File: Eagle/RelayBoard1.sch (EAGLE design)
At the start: 12 parts, among them IC1 ULN2003AN, J1 POWER, J2 CPU_BOARD, K1 4052, K2 4052, K3 4051, X1 MKDSN1,5/6-5,08, X2 MKDSN1,5/6-5,08, X4 MKDSN1,5/3-5,08

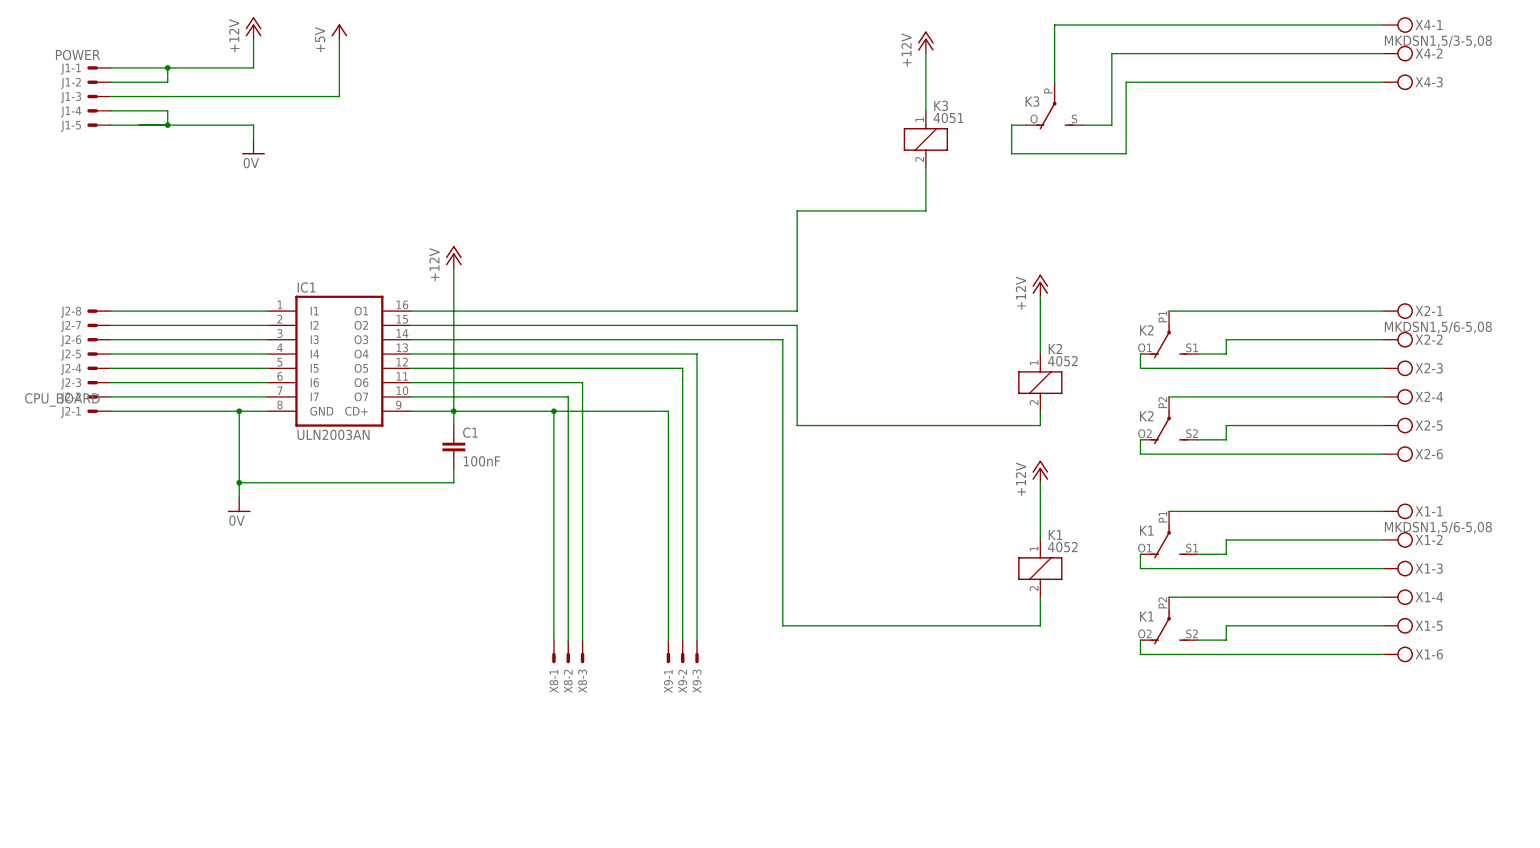
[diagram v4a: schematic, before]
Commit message: - cabling of RelayBoard1 partly changed - some pin-swaps to ButtonBoard -> blrtest.c finally works as expected
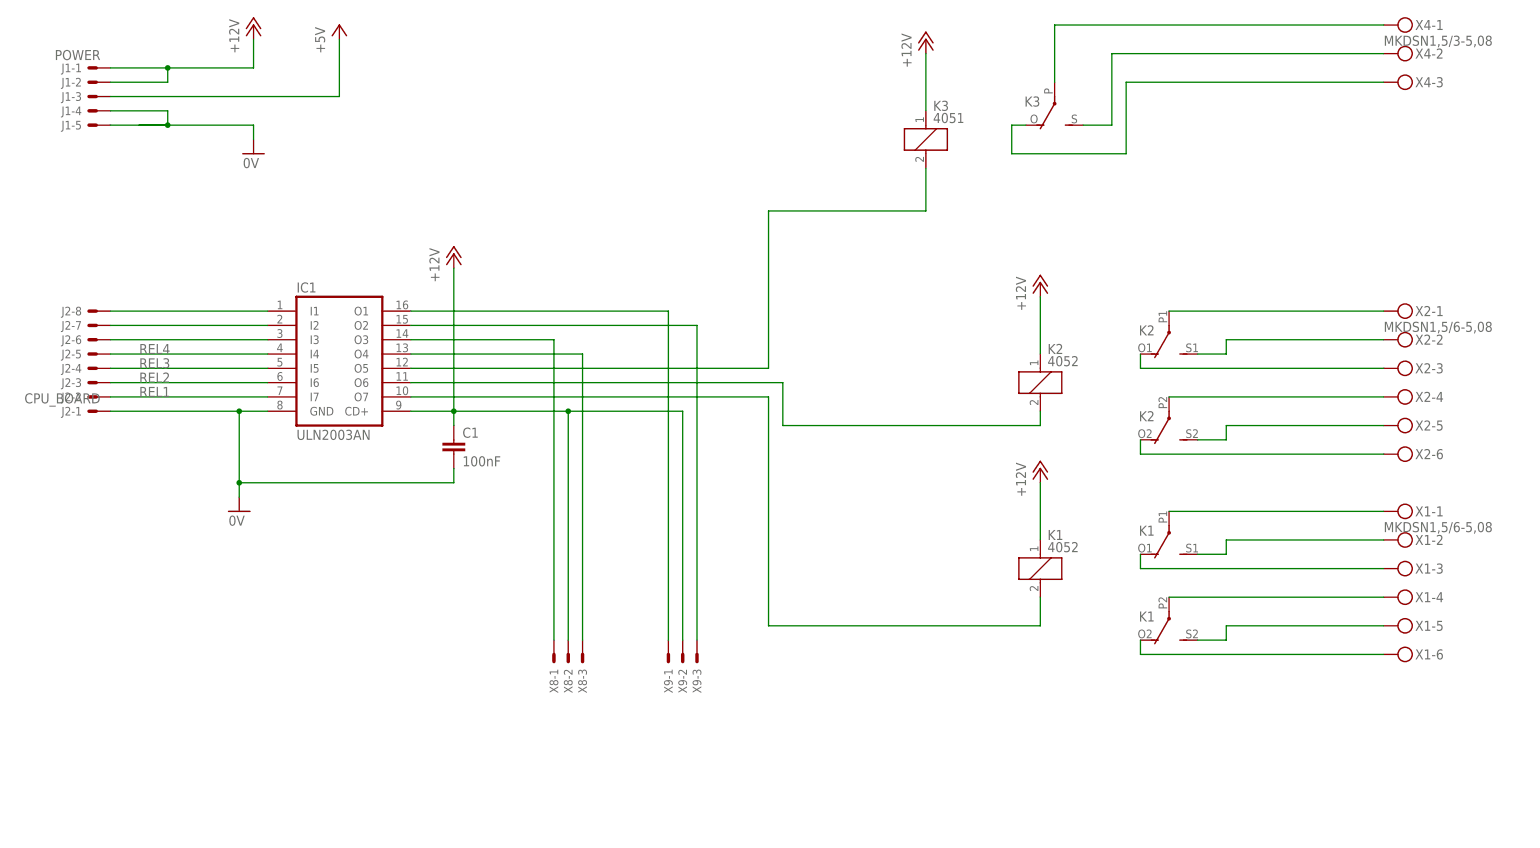
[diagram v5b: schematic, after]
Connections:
- net N$20 renamed REL4
- net N$21 renamed REL3
- net N$22 renamed REL2
- net N$23 renamed REL1
- net +12V: now also X8-2.S, X9-2.S; no longer X8-1.S, X9-1.S
- net N$25: now also IC1.O6; no longer IC1.O2
- net N$26: now also IC1.O5, K31.2; no longer IC1.O3, K11.2
- net N$27: now also IC1.O3, X8-1.S; no longer IC1.O6, X8-3.S
- net N$28: now also IC1.O4, X8-3.S; no longer IC1.O7, X8-2.S
- net N$29: now also IC1.O1, X9-1.S; no longer IC1.O4, X9-3.S
- net N$30: now also IC1.O2, X9-3.S; no longer IC1.O5, X9-2.S
- net N$4: now also IC1.O7, K11.2; no longer IC1.O1, K31.2
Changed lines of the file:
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@@
 <wire x1="78.74" y1="88.9" x2="78.74" y2="91.44" width="0.1524" layer="91"/>
 <wire x1="78.74" y1="88.9" x2="40.64" y2="88.9" width="0.1524" layer="91"/>
-<pinref part="IC1" gate="A" pin="GND"/>
-<wire x1="45.72" y1="101.6" x2="40.64" y2="101.6" width="0.1524" layer="91"/>
-<wire x1="40.64" y1="88.9" x2="40.64" y2="101.6" width="0.1524" layer="91"/>
 <pinref part="GND2" gate="1" pin="0V"/>
 <wire x1="40.64" y1="86.36" x2="40.64" y2="88.9" width="0.1524" layer="91"/>
 <junction x="40.64" y="88.9"/>
+<wire x1="40.64" y1="88.9" x2="40.64" y2="101.6" width="0.1524" layer="91"/>
 <pinref part="J2" gate="-1" pin="S"/>
-<wire x1="40.64" y1="101.6" x2="17.78" y2="101.6" width="0.1524" layer="91"/>
+<wire x1="17.78" y1="101.6" x2="40.64" y2="101.6" width="0.1524" layer="91"/>
+<pinref part="IC1" gate="A" pin="GND"/>
+<wire x1="40.64" y1="101.6" x2="45.72" y2="101.6" width="0.1524" layer="91"/>
 <junction x="40.64" y="101.6"/>
 </segment>
@@
 <wire x1="78.74" y1="101.6" x2="71.12" y2="101.6" width="0.1524" layer="91"/>
 <junction x="78.74" y="101.6"/>
-<wire x1="78.74" y1="101.6" x2="96.52" y2="101.6" width="0.1524" layer="91"/>
-<pinref part="X9" gate="-1" pin="S"/>
-<wire x1="96.52" y1="101.6" x2="116.84" y2="101.6" width="0.1524" layer="91"/>
-<wire x1="116.84" y1="101.6" x2="116.84" y2="60.96" width="0.1524" layer="91"/>
-<pinref part="X8" gate="-1" pin="S"/>
-<wire x1="96.52" y1="101.6" x2="96.52" y2="60.96" width="0.1524" layer="91"/>
-<junction x="96.52" y="101.6"/>
+<wire x1="78.74" y1="101.6" x2="99.06" y2="101.6" width="0.1524" layer="91"/>
+<pinref part="X8" gate="-2" pin="S"/>
+<wire x1="99.06" y1="60.96" x2="99.06" y2="101.6" width="0.1524" layer="91"/>
+<wire x1="99.06" y1="101.6" x2="119.38" y2="101.6" width="0.1524" layer="91"/>
+<junction x="99.06" y="101.6"/>
+<pinref part="X9" gate="-2" pin="S"/>
+<wire x1="119.38" y1="101.6" x2="119.38" y2="60.96" width="0.1524" layer="91"/>
 </segment>
 </net>
 <net name="N$4" class="0">
 <segment>
-<pinref part="IC1" gate="A" pin="O1"/>
-<wire x1="71.12" y1="119.38" x2="139.7" y2="119.38" width="0.1524" layer="91"/>
-<wire x1="139.7" y1="119.38" x2="139.7" y2="137.16" width="0.1524" layer="91"/>
-<wire x1="139.7" y1="137.16" x2="162.56" y2="137.16" width="0.1524" layer="91"/>
-<pinref part="K3" gate="1" pin="2"/>
-<wire x1="162.56" y1="137.16" x2="162.56" y2="144.78" width="0.1524" layer="91"/>
+<pinref part="IC1" gate="A" pin="O7"/>
+<wire x1="71.12" y1="104.14" x2="134.62" y2="104.14" width="0.1524" layer="91"/>
+<pinref part="K1" gate="1" pin="2"/>
+<wire x1="182.88" y1="63.5" x2="182.88" y2="68.58" width="0.1524" layer="91"/>
+<wire x1="134.62" y1="63.5" x2="182.88" y2="63.5" width="0.1524" layer="91"/>
+<wire x1="134.62" y1="104.14" x2="134.62" y2="63.5" width="0.1524" layer="91"/>
 </segment>
 </net>
 <net name="N$25" class="0">
 <segment>
-<pinref part="IC1" gate="A" pin="O2"/>
-<wire x1="71.12" y1="116.84" x2="139.7" y2="116.84" width="0.1524" layer="91"/>
-<wire x1="139.7" y1="116.84" x2="139.7" y2="99.06" width="0.1524" layer="91"/>
-<wire x1="139.7" y1="99.06" x2="182.88" y2="99.06" width="0.1524" layer="91"/>
+<pinref part="IC1" gate="A" pin="O6"/>
+<wire x1="71.12" y1="106.68" x2="137.16" y2="106.68" width="0.1524" layer="91"/>
 <pinref part="K2" gate="1" pin="2"/>
+<wire x1="137.16" y1="99.06" x2="182.88" y2="99.06" width="0.1524" layer="91"/>
 <wire x1="182.88" y1="99.06" x2="182.88" y2="101.6" width="0.1524" layer="91"/>
+<wire x1="137.16" y1="106.68" x2="137.16" y2="99.06" width="0.1524" layer="91"/>
 </segment>
 </net>
 <net name="N$26" class="0">
 <segment>
-<pinref part="IC1" gate="A" pin="O3"/>
-<wire x1="71.12" y1="114.3" x2="137.16" y2="114.3" width="0.1524" layer="91"/>
-<wire x1="137.16" y1="114.3" x2="137.16" y2="63.5" width="0.1524" layer="91"/>
-<wire x1="137.16" y1="63.5" x2="182.88" y2="63.5" width="0.1524" layer="91"/>
-<pinref part="K1" gate="1" pin="2"/>
-<wire x1="182.88" y1="63.5" x2="182.88" y2="68.58" width="0.1524" layer="91"/>
+<pinref part="IC1" gate="A" pin="O5"/>
+<wire x1="71.12" y1="109.22" x2="134.62" y2="109.22" width="0.1524" layer="91"/>
+<wire x1="134.62" y1="109.22" x2="134.62" y2="137.16" width="0.1524" layer="91"/>
+<pinref part="K3" gate="1" pin="2"/>
+<wire x1="162.56" y1="137.16" x2="162.56" y2="144.78" width="0.1524" layer="91"/>
+<wire x1="134.62" y1="137.16" x2="162.56" y2="137.16" width="0.1524" layer="91"/>
 </segment>
 </net>
 <net name="N$27" class="0">
 <segment>
-<pinref part="IC1" gate="A" pin="O6"/>
-<pinref part="X8" gate="-3" pin="S"/>
-<wire x1="71.12" y1="106.68" x2="101.6" y2="106.68" width="0.1524" layer="91"/>
-<wire x1="101.6" y1="106.68" x2="101.6" y2="60.96" width="0.1524" layer="91"/>
+<pinref part="IC1" gate="A" pin="O3"/>
+<pinref part="X8" gate="-1" pin="S"/>
+<wire x1="96.52" y1="114.3" x2="71.12" y2="114.3" width="0.1524" layer="91"/>
+<wire x1="96.52" y1="60.96" x2="96.52" y2="114.3" width="0.1524" layer="91"/>
 </segment>
 </net>
 <net name="N$28" class="0">
 <segment>
-<pinref part="X8" gate="-2" pin="S"/>
-<wire x1="99.06" y1="60.96" x2="99.06" y2="104.14" width="0.1524" layer="91"/>
-<pinref part="IC1" gate="A" pin="O7"/>
-<wire x1="99.06" y1="104.14" x2="71.12" y2="104.14" width="0.1524" layer="91"/>
+<pinref part="IC1" gate="A" pin="O4"/>
+<wire x1="101.6" y1="111.76" x2="71.12" y2="111.76" width="0.1524" layer="91"/>
+<pinref part="X8" gate="-3" pin="S"/>
+<wire x1="101.6" y1="60.96" x2="101.6" y2="111.76" width="0.1524" layer="91"/>
 </segment>
 </net>
 <net name="N$29" class="0">
 <segment>
-<pinref part="IC1" gate="A" pin="O4"/>
-<pinref part="X9" gate="-3" pin="S"/>
-<wire x1="71.12" y1="111.76" x2="121.92" y2="111.76" width="0.1524" layer="91"/>
-<wire x1="121.92" y1="111.76" x2="121.92" y2="60.96" width="0.1524" layer="91"/>
+<pinref part="IC1" gate="A" pin="O1"/>
+<wire x1="71.12" y1="119.38" x2="116.84" y2="119.38" width="0.1524" layer="91"/>
+<pinref part="X9" gate="-1" pin="S"/>
+<wire x1="116.84" y1="60.96" x2="116.84" y2="119.38" width="0.1524" layer="91"/>
 </segment>
 </net>
 <net name="N$30" class="0">
 <segment>
-<pinref part="IC1" gate="A" pin="O5"/>
-<pinref part="X9" gate="-2" pin="S"/>
-<wire x1="71.12" y1="109.22" x2="119.38" y2="109.22" width="0.1524" layer="91"/>
-<wire x1="119.38" y1="109.22" x2="119.38" y2="60.96" width="0.1524" layer="91"/>
+<pinref part="IC1" gate="A" pin="O2"/>
+<wire x1="121.92" y1="116.84" x2="71.12" y2="116.84" width="0.1524" layer="91"/>
+<pinref part="X9" gate="-3" pin="S"/>
+<wire x1="121.92" y1="116.84" x2="121.92" y2="60.96" width="0.1524" layer="91"/>
 </segment>
 </net>
@@
 </segment>
 </net>
-<net name="N$5" class="0">
+<net name="REL1" class="0">
 <segment>
-<pinref part="J2" gate="-8" pin="S"/>
-<pinref part="IC1" gate="A" pin="I1"/>
-<wire x1="17.78" y1="119.38" x2="45.72" y2="119.38" width="0.1524" layer="91"/>
+<pinref part="IC1" gate="A" pin="I7"/>
+<pinref part="J2" gate="-2" pin="S"/>
+<wire x1="45.72" y1="104.14" x2="17.78" y2="104.14" width="0.1524" layer="91"/>
+<label x="22.86" y="104.14" size="1.778" layer="95"/>
 </segment>
 </net>
-<net name="N$18" class="0">
+<net name="REL2" class="0">
 <segment>
-<pinref part="IC1" gate="A" pin="I2"/>
-<pinref part="J2" gate="-7" pin="S"/>
-<wire x1="45.72" y1="116.84" x2="17.78" y2="116.84" width="0.1524" layer="91"/>
+<pinref part="J2" gate="-3" pin="S"/>
+<pinref part="IC1" gate="A" pin="I6"/>
+<wire x1="17.78" y1="106.68" x2="45.72" y2="106.68" width="0.1524" layer="91"/>
+<label x="22.86" y="106.68" size="1.778" layer="95"/>
 </segment>
 </net>
-<net name="N$19" class="0">
+<net name="REL3" class="0">
 <segment>
-<pinref part="J2" gate="-6" pin="S"/>
-<pinref part="IC1" gate="A" pin="I3"/>
-<wire x1="17.78" y1="114.3" x2="45.72" y2="114.3" width="0.1524" layer="91"/>
+<pinref part="IC1" gate="A" pin="I5"/>
+<pinref part="J2" gate="-4" pin="S"/>
+<wire x1="45.72" y1="109.22" x2="17.78" y2="109.22" width="0.1524" layer="91"/>
+<label x="22.86" y="109.22" size="1.778" layer="95"/>
 </segment>
 </net>
-<net name="N$20" class="0">
+<net name="REL4" class="0">
 <segment>
+<pinref part="J2" gate="-5" pin="S"/>
 <pinref part="IC1" gate="A" pin="I4"/>
-<pinref part="J2" gate="-5" pin="S"/>
-<wire x1="45.72" y1="111.76" x2="17.78" y2="111.76" width="0.1524" layer="91"/>
+<wire x1="17.78" y1="111.76" x2="45.72" y2="111.76" width="0.1524" layer="91"/>
+<label x="22.86" y="111.76" size="1.778" layer="95"/>
 </segment>
 </net>
 <net name="N$21" class="0">
 <segment>
-<pinref part="J2" gate="-4" pin="S"/>
-<pinref part="IC1" gate="A" pin="I5"/>
-<wire x1="17.78" y1="109.22" x2="45.72" y2="109.22" width="0.1524" layer="91"/>
+<pinref part="IC1" gate="A" pin="I3"/>
+<pinref part="J2" gate="-6" pin="S"/>
+<wire x1="45.72" y1="114.3" x2="17.78" y2="114.3" width="0.1524" layer="91"/>
 </segment>
 </net>
 <net name="N$22" class="0">
 <segment>
-<pinref part="IC1" gate="A" pin="I6"/>
-<pinref part="J2" gate="-3" pin="S"/>
-<wire x1="45.72" y1="106.68" x2="17.78" y2="106.68" width="0.1524" layer="91"/>
+<pinref part="J2" gate="-7" pin="S"/>
+<pinref part="IC1" gate="A" pin="I2"/>
+<wire x1="17.78" y1="116.84" x2="45.72" y2="116.84" width="0.1524" layer="91"/>
 </segment>
 </net>
 <net name="N$23" class="0">
 <segment>
-<pinref part="J2" gate="-2" pin="S"/>
-<pinref part="IC1" gate="A" pin="I7"/>
-<wire x1="17.78" y1="104.14" x2="45.72" y2="104.14" width="0.1524" layer="91"/>
+<pinref part="IC1" gate="A" pin="I1"/>
+<pinref part="J2" gate="-8" pin="S"/>
+<wire x1="45.72" y1="119.38" x2="17.78" y2="119.38" width="0.1524" layer="91"/>
 </segment>
 </net>
